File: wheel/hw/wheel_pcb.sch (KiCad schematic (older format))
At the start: 36 parts, among them J1 LCD, J2 DEBUG, J3 LCD_BL, J4 CAR, SW1 CONFIG, U1 LPC11C24FBD48, U2 TPS62175, U3 TLV70233_SOT23-5, Y1 12MHz

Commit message: remove dashboard specific parts
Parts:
- removed J3: LCD_BL, Pin_Headers:Pin_Header_Angled_1x03_Pitch2.54mm, symbol Conn_01x03
- removed R11, R12: 36, Resistors_SMD:R_1206, symbol R
- removed RV1: 10k, custom_footprints:Bourns_3362X, symbol POT
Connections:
- net labels removed: LCD_LED_A, LCD_LED_K
- wire segments 114 -> 106
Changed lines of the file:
@@
 $EndComp
-$Comp
-L Conn_01x03 J3
-U 1 1 5AE5C0EF
-P 10750 2950
-F 0 "J3" H 10750 3150 50  0000 C CNN
-F 1 "LCD_BL" H 10750 2750 50  0000 C CNN
-F 2 "Pin_Headers:Pin_Header_Angled_1x03_Pitch2.54mm" H 10750 2950 50  0001 C CNN
-F 3 "https://www.mouser.de/ProductDetail/TE-Connectivity-AMP/281698-3?qs=sGAEpiMZZMs%252bGHln7q6pm5RYho2xCXYA8YIXmNK49H8%3d" H 10750 2950 50  0001 C CNN
-	1    10750 2950
-	1    0    0    -1
-$EndComp
-$Comp
-L POT RV1
-U 1 1 5AE5C369
-P 10550 3600
-F 0 "RV1" V 10375 3600 50  0000 C CNN
-F 1 "10k" V 10450 3600 50  0000 C CNN
-F 2 "custom_footprints:Bourns_3362X" H 10550 3600 50  0001 C CNN
-F 3 "https://www.mouser.de/ProductDetail/Bourns/3362X-1-103LF?qs=sGAEpiMZZMtC25l1F4XBUxECHfqDmxl1ITAi%252bn07c9o%3d" H 10550 3600 50  0001 C CNN
-	1    10550 3600
-	0    -1   -1   0
-$EndComp
-$Comp
-L GND #PWR011
-U 1 1 5AE5C42C
-P 10850 3600
-F 0 "#PWR011" H 10850 3350 50  0001 C CNN
-F 1 "GND" H 10850 3450 50  0000 C CNN
-F 2 "" H 10850 3600 50  0001 C CNN
-F 3 "" H 10850 3600 50  0001 C CNN
-	1    10850 3600
-	1    0    0    -1
-$EndComp
-Text Label 10550 3450 0    60   ~ 0
-LCD_V0
-Text Label 10400 3600 2    60   ~ 0
-LCD_VEE
 $Comp
 L R R2
@@
 XTALOUT
 $Comp
-L GND #PWR024
-U 1 1 5AF17E60
-P 10500 3100
-F 0 "#PWR024" H 10500 2850 50  0001 C CNN
-F 1 "GND" H 10500 2950 50  0000 C CNN
-F 2 "" H 10500 3100 50  0001 C CNN
-F 3 "" H 10500 3100 50  0001 C CNN
-	1    10500 3100
-	1    0    0    -1
-$EndComp
-Text Label 10500 3050 2    60   ~ 0
-LCD_LED_K
-Text Label 10500 2850 2    60   ~ 0
-LCD_LED_A
-$Comp
-L R R11
-U 1 1 5AF1A31D
-P 10600 2500
-F 0 "R11" V 10680 2500 50  0000 C CNN
-F 1 "36" V 10600 2500 50  0000 C CNN
-F 2 "Resistors_SMD:R_1206" V 10530 2500 50  0001 C CNN
-F 3 "https://www.mouser.de/ProductDetail/Vishay/CRCW120636R0FKEA?qs=sGAEpiMZZMtlubZbdhIBIIDYYWLC5QWgMrFcVuisbCE%3d" H 10600 2500 50  0001 C CNN
-	1    10600 2500
-	1    0    0    -1
-$EndComp
-$Comp
-L +5V #PWR025
-U 1 1 5AF1A42C
-P 10500 2300
-F 0 "#PWR025" H 10500 2150 50  0001 C CNN
-F 1 "+5V" H 10500 2440 50  0000 C CNN
-F 2 "" H 10500 2300 50  0001 C CNN
-F 3 "" H 10500 2300 50  0001 C CNN
-	1    10500 2300
-	1    0    0    -1
-$EndComp
-$Comp
 L +BATT #PWR026
 U 1 1 5AF2F5B2
@@
 Text Label 8050 4300 0    60   ~ 0
 CANL
-$Comp
-L R R12
-U 1 1 5AF38BC5
-P 10400 2500
-F 0 "R12" V 10480 2500 50  0000 C CNN
-F 1 "36" V 10400 2500 50  0000 C CNN
-F 2 "Resistors_SMD:R_1206" V 10330 2500 50  0001 C CNN
-F 3 "https://www.mouser.de/ProductDetail/Vishay/CRCW120636R0FKEA?qs=sGAEpiMZZMtlubZbdhIBIIDYYWLC5QWgMrFcVuisbCE%3d" H 10400 2500 50  0001 C CNN
-	1    10400 2500
-	1    0    0    -1
-$EndComp
 Text Label 3200 1900 0    60   ~ 0
 MCU_~RESET
@@
 	8450 3100 9000 3100
 Wire Wire Line
-	10700 3600 10850 3600
-Wire Wire Line
 	7750 4200 7750 4350
 Connection ~ 7750 4200
@@
 Connection ~ 6800 5600
 Wire Wire Line
-	10500 3050 10550 3050
-Wire Wire Line
-	10500 2850 10550 2850
-Wire Wire Line
-	10500 2650 10500 2850
-Wire Wire Line
-	10500 3100 10500 3050
-Wire Wire Line
 	1150 750  1650 750
 Wire Wire Line
@@
 	1550 1050 1550 1500
 Wire Wire Line
-	10400 2350 10600 2350
-Wire Wire Line
-	10500 2350 10500 2300
-Connection ~ 10500 2350
-Wire Wire Line
-	10400 2650 10600 2650
-Connection ~ 10500 2650
-Wire Wire Line
 	2950 1500 2950 1900

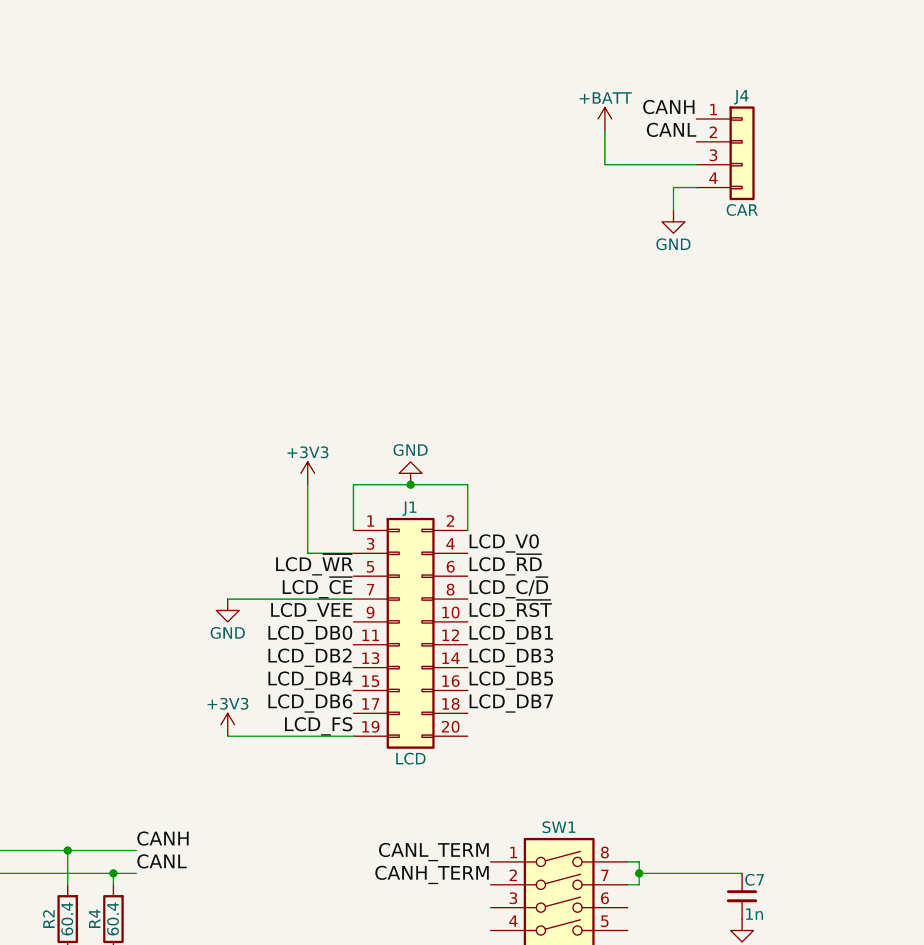
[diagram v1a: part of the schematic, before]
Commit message: preliminarily lay out and pin wheel connectors
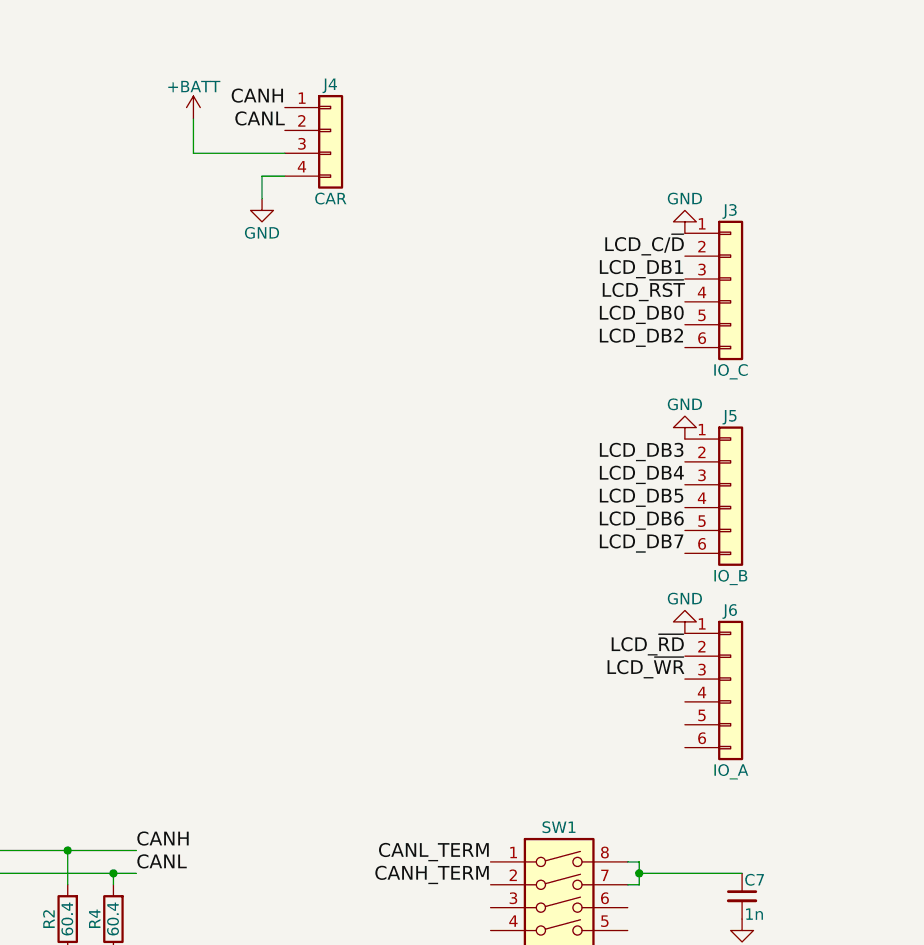
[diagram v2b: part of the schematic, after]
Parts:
- removed J1: LCD, Socket_Strips:Socket_Strip_Straight_2x10_Pitch2.54mm, symbol Conn_02x10_Odd_Even
- added J3: IO_C, Pin_Headers:Pin_Header_Angled_1x06_Pitch2.54mm, symbol Conn_01x06
- added J5: IO_B, Pin_Headers:Pin_Header_Angled_1x06_Pitch2.54mm, symbol Conn_01x06
- added J6: IO_A, Pin_Headers:Pin_Header_Angled_1x06_Pitch2.54mm, symbol Conn_01x06
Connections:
- net GND: now also J3.1 (Pin_1), J5.1 (Pin_1), J6.1 (Pin_1)
- net LCD_C/~D: now also J3.2 (Pin_2)
- net LCD_DB0: now also J3.5 (Pin_5)
- net LCD_DB1: now also J3.3 (Pin_3)
- net LCD_DB2: now also J3.6 (Pin_6)
- net LCD_DB3: now also J5.2 (Pin_2)
- net LCD_DB4: now also J5.3 (Pin_3)
- net LCD_DB5: now also J5.4 (Pin_4)
- net LCD_DB6: now also J5.5 (Pin_5)
- net LCD_DB7: now also J5.6 (Pin_6)
- net LCD_~RD: now also J6.2 (Pin_2)
- net LCD_~RST: now also J3.4 (Pin_4)
- net LCD_~WR: now also J6.3 (Pin_3)
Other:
- moved on the sheet: J4

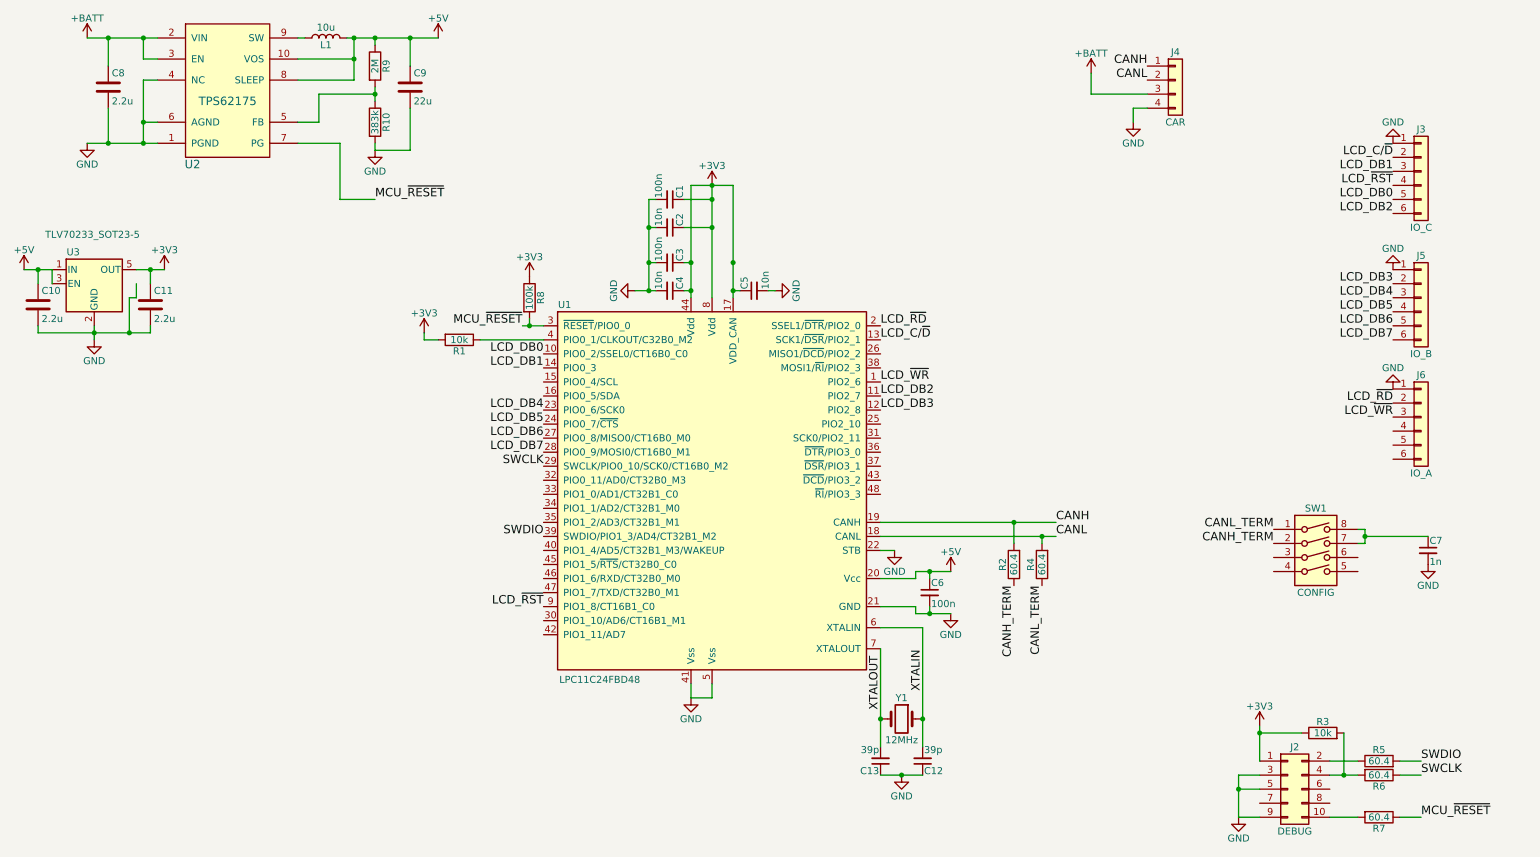
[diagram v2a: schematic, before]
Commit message: relabel i/o with less lcd names
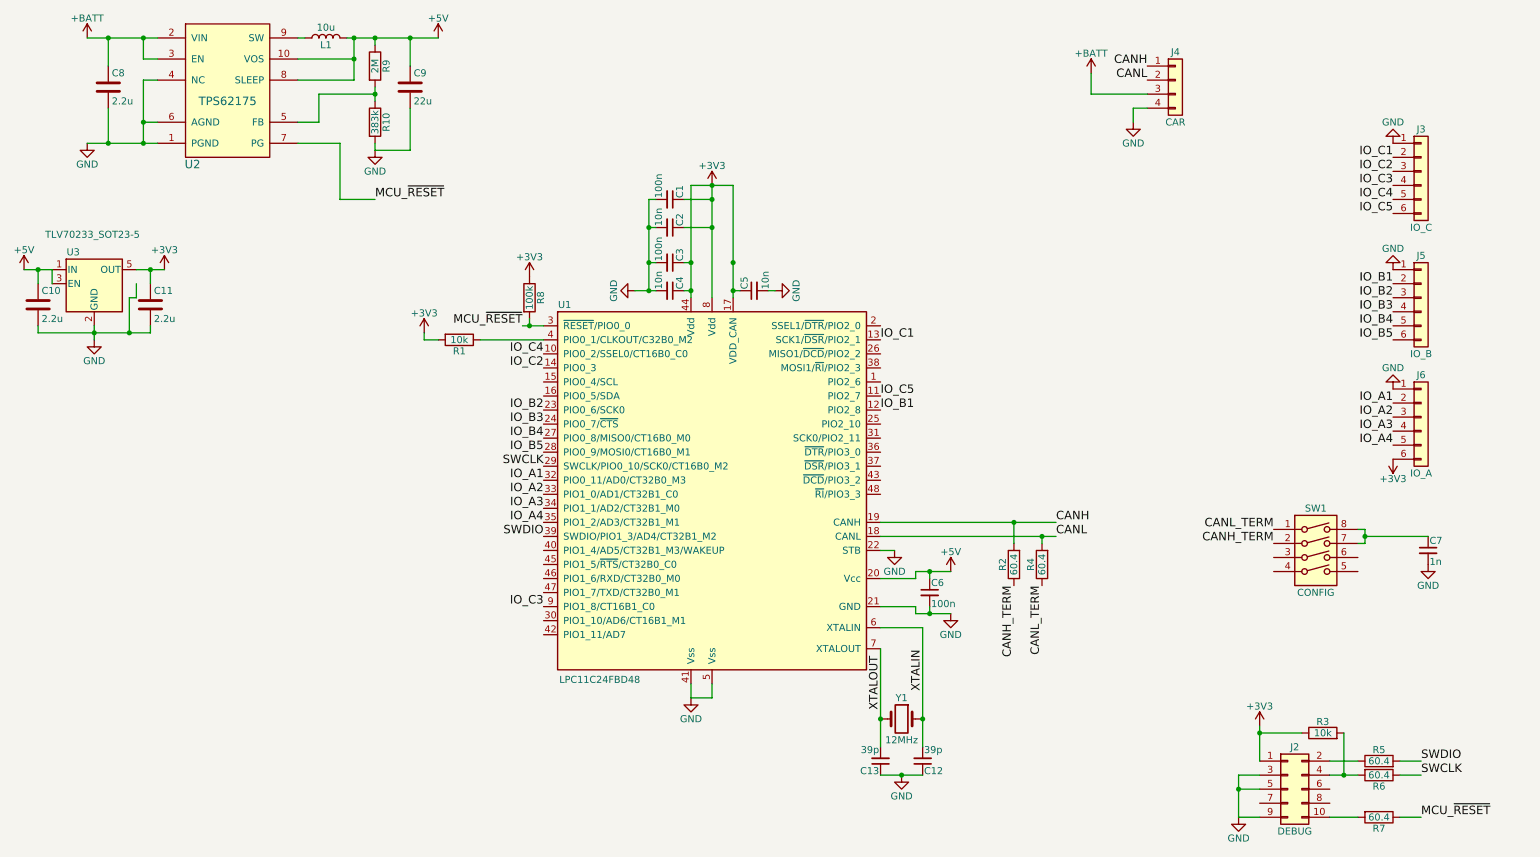
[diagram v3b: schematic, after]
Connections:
- net +3V3: now also J6.6 (Pin_6)
- net IO_A1: now reaches U1.32 (PIO0_11/AD0/CT32B0_M3)
- net IO_A1: now also J6.2 (Pin_2)
- net IO_A2: now reaches U1.33 (PIO1_0/AD1/CT32B1_C0)
- net IO_A2: now also J6.3 (Pin_3)
- net IO_A3: now reaches U1.34 (PIO1_1/AD2/CT32B1_M0)
- net IO_A3: now also J6.4 (Pin_4)
- net IO_A4: now reaches U1.35 (PIO1_2/AD3/CT32B1_M1)
- net IO_A4: now also J6.5 (Pin_5)
- net LCD_C/~D renamed IO_C1
- net LCD_DB0 renamed IO_C4
- net LCD_DB1 renamed IO_C2
- net LCD_DB2 renamed IO_C5
- net LCD_DB3 renamed IO_B1
- net LCD_DB4 renamed IO_B2
- net LCD_DB5 renamed IO_B3
- net LCD_DB6 renamed IO_B4
- net LCD_DB7 renamed IO_B5
- net LCD_~RD: no longer names the net of U1.2 (SSEL1/~DTR~/PIO2_0)
- net LCD_~RD: no longer J6.2 (Pin_2)
- net LCD_~RST renamed IO_C3
- net LCD_~WR: no longer names the net of U1.1 (PIO2_6)
- net LCD_~WR: no longer J6.3 (Pin_3)
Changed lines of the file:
@@
 $EndComp
 Text Label 4400 3000 2    60   ~ 0
-LCD_DB0
+IO_C4
 Text Label 4400 3100 2    60   ~ 0
-LCD_DB1
+IO_C2
 Text Label 6800 3300 0    60   ~ 0
-LCD_DB2
+IO_C5
 Text Label 6800 3400 0    60   ~ 0
-LCD_DB3
+IO_B1
 Text Label 4400 3400 2    60   ~ 0
-LCD_DB4
+IO_B2
 Text Label 4400 3500 2    60   ~ 0
-LCD_DB5
+IO_B3
 Text Label 4400 3600 2    60   ~ 0
-LCD_DB6
+IO_B4
 Text Label 4400 3700 2    60   ~ 0
-LCD_DB7
+IO_B5
 Text Label 4400 3800 2    60   ~ 0
 SWCLK
@@
 Text Label 10650 6000 0    60   ~ 0
 SWCLK
-Text Label 6800 2900 0    60   ~ 0
-LCD_C/~D
 Text Label 4400 4800 2    60   ~ 0
-LCD_~RST
-Text Label 6800 3200 0    60   ~ 0
-LCD_~WR
-Text Label 6800 2800 0    60   ~ 0
-LCD_~RD
+IO_C3
 $Comp
 L R R2
@@
 	-1   0    0    1
 $EndComp
+Text Label 10450 1700 2    60   ~ 0
+IO_C2
+Text Label 10450 1800 2    60   ~ 0
+IO_C3
+Text Label 10450 1900 2    60   ~ 0
+IO_C4
+Text Label 10450 2000 2    60   ~ 0
+IO_C5
+Text Label 10450 2500 2    60   ~ 0
+IO_B1
+Text Label 10450 2600 2    60   ~ 0
+IO_B2
+Text Label 10450 2700 2    60   ~ 0
+IO_B3
+Text Label 10450 2800 2    60   ~ 0
+IO_B4
+Text Label 10450 2900 2    60   ~ 0
+IO_B5
+Text Label 10450 3350 2    60   ~ 0
+IO_A1
+Text Label 10450 3450 2    60   ~ 0
+IO_A2
 Text Label 10450 1600 2    60   ~ 0
-LCD_C/~D
-Text Label 10450 1700 2    60   ~ 0
-LCD_DB1
-Text Label 10450 1800 2    60   ~ 0
-LCD_~RST
-Text Label 10450 1900 2    60   ~ 0
-LCD_DB0
-Text Label 10450 2000 2    60   ~ 0
-LCD_DB2
-Text Label 10450 2500 2    60   ~ 0
-LCD_DB3
-Text Label 10450 2600 2    60   ~ 0
-LCD_DB4
-Text Label 10450 2700 2    60   ~ 0
-LCD_DB5
-Text Label 10450 2800 2    60   ~ 0
-LCD_DB6
-Text Label 10450 2900 2    60   ~ 0
-LCD_DB7
-Text Label 10450 3350 2    60   ~ 0
-LCD_~RD
-Text Label 10450 3450 2    60   ~ 0
-LCD_~WR
+IO_C1
+Text Label 6800 2900 0    60   ~ 0
+IO_C1
+Text Label 10450 3550 2    60   ~ 0
+IO_A3
+Text Label 10450 3650 2    60   ~ 0
+IO_A4
+$Comp
+L +3V3 #PWR?
+U 1 1 5B00156F
+P 10450 3750
+F 0 "#PWR?" H 10450 3600 50  0001 C CNN
+F 1 "+3V3" H 10450 3890 50  0000 C CNN
+F 2 "" H 10450 3750 50  0001 C CNN
+F 3 "" H 10450 3750 50  0001 C CNN
+	1    10450 3750
+	-1   0    0    1
+$EndComp
+Text Label 4400 3900 2    60   ~ 0
+IO_A1
+Text Label 4400 4000 2    60   ~ 0
+IO_A2
+Text Label 4400 4100 2    60   ~ 0
+IO_A3
+Text Label 4400 4200 2    60   ~ 0
+IO_A4
 $EndSCHEMATC

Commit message: add protection circuitry
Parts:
- added C14, C15, C16, C17: 100n, Capacitors_SMD:C_0603, symbol C
- added D1: SS14, Diodes_SMD:D_SMA_Handsoldering, symbol D
- added D2: SMLJ22A-Q, Diodes_SMD:D_SMC, symbol D_Zener
- added D3: PESD1CAN-U, TO_SOT_Packages_SMD:SOT-23, symbol D_TVS_x2_AAC
- added U4, U5: SP4065-08ATG, Housings_SSOP:MSOP-10_3x3mm_Pitch0.5mm, symbol Conn_02x05_Counter_Clockwise
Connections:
- net +3V3: now also C15.1
- net +5V: now also C14.1, C17.1
- net +BATT: now also D1.2 (A); no longer C8.1, U2.2 (VIN), U2.3 (EN)
- net CANH: now also D3.1 (A1)
- net CANL: now also D3.2 (A2)
- net GND: now also C14.2, C15.2, C16.2, C17.2, D2.2 (A), D3.3 (common), U4.6 (Pin_6), U5.6 (Pin_6)
- net IO_A1: now also U5.3 (Pin_3)
- net IO_A2: now also U5.4 (Pin_4)
- net IO_A3: now also U5.10 (Pin_10)
- net IO_A4: now also U5.9 (Pin_9)
- net IO_B1: now also U4.9 (Pin_9)
- net IO_B2: now also U4.8 (Pin_8)
- net IO_B3: now also U4.7 (Pin_7)
- net IO_B4: now also U5.1 (Pin_1)
- net IO_B5: now also U5.2 (Pin_2)
- net IO_C1: now also U4.1 (Pin_1)
- net IO_C2: now also U4.2 (Pin_2)
- net IO_C3: now also U4.3 (Pin_3)
- net IO_C4: now also U4.4 (Pin_4)
- net IO_C5: now also U4.10 (Pin_10)
- new net: C16.1, C8.1, D1.1 (K), D2.1 (K), U2.2 (VIN), U2.3 (EN)
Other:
- moved on the sheet: C11, C8, C9, L1, R10, R9, U2, U3
